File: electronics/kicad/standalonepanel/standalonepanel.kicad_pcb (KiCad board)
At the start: 2 copper layers, 135 x 54 mm, 81 parts, among them J1 Speaker, J2 POWER, P1 USB-C, P2 USB-A, SW1 TST-ESP32, SW2 BOOT, SW3 TST-ICE40, SW4 RESET, U1 SC189ZSKTRT, U10 MPU-6050, U2 SC189ZSKTRT, U3 ESP32-WROVER-E, U4 CH340C, U5 MAX3421E, U6 IS64WV25616EFBLL-10TLI, U7 ICE40-HX4K, U9 MAX98357A, X2 12MHz

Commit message: electronics & PCB v1
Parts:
- added BT1: CR2032, 0_project:cr2032_smd_clip, F.Cu at (120.7, 99.3)
- added C14: 100nF, Capacitor_SMD:C_0805_2012Metric_Pad1.18x1.45mm_HandSolder, B.Cu at (151.5, 117.5)
- added R9: 10K, Resistor_SMD:R_1206_3216Metric_Pad1.30x1.75mm_HandSolder, B.Cu at (116.7, 128.1)
- added U8: DS3231M, Package_SO:SO-16_3.9x9.9mm_P1.27mm, F.Cu at (151.0, 117.5)
- moved G*** 33.0 mm to (100.6, 106.0)
- moved C27 25.7 mm to (141.8, 114.8), turned to 90 degrees
- moved R15 22.5 mm to (137.8, 114.0)
- moved SW4 12.6 mm to (137.7, 110.4), turned to 180 degrees
- moved LED3 2.83 mm to (137.6, 117.5)
- moved LED1 2.77 mm to (137.7, 123.4)
- moved R5 2.62 mm to (137.8, 126.0)
- moved R8 2.46 mm to (137.7, 120.0)
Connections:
- net /DSP1_B1 renamed DSP1-B1
- net /DSP1_B2 renamed DSP1-B2
- net /DSP1_G1 renamed DSP1-G1
- net /DSP1_G2 renamed DSP1-G2
- net /DSP1_R1 renamed DSP1-R1
- net /DSP1_R2 renamed DSP1-R2
- net /DSP2_B1 renamed DSP2-B1
- net /DSP2_B2 renamed DSP2-B2
- net /DSP2_G1 renamed DSP2-G1
- net /DSP2_G2 renamed DSP2-G2
- net /DSP2_R1 renamed DSP2-R1
- net /DSP2_R2 renamed DSP2-R2
- net /DSP_A renamed DSP-A
- net /DSP_B renamed DSP-B
- net /DSP_C renamed DSP-C
- net /DSP_CLK renamed DSP-CLK
- net /DSP_D renamed DSP-D
- net /DSP_E renamed DSP-E
- net /DSP_LAT renamed DSP-LAT
- net /DSP_OE renamed DSP-OE
- net /HSPI-CLK renamed HSPI-CLK
- net /HSPI-CS-USB renamed HSPI-CS-USB
- net /HSPI-SDI renamed HSPI-SDI
- net /HSPI-SDO renamed HSPI-SDO
- net /HSPI_INT renamed HSPI-INT
- net /I2C-CLK renamed I2C-CLK
- net /I2C-SDA renamed I2C-SDA
- net /ICE40-CDONE renamed Net-(LED4-A)
- net /RAM-A0 renamed RAM-A0
- net /RAM-A1 renamed RAM-A1
- net /RAM-A10 renamed RAM-A10
- net /RAM-A11 renamed RAM-A11
- net /RAM-A12 renamed RAM-A12
- net /RAM-A13 renamed RAM-A13
- net /RAM-A14 renamed RAM-A14
- net /RAM-A15 renamed RAM-A15
- net /RAM-A16 renamed RAM-A16
- net /RAM-A17 renamed RAM-A17
- net /RAM-A2 renamed RAM-A2
- net /RAM-A3 renamed RAM-A3
- net /RAM-A4 renamed RAM-A4
- net /RAM-A5 renamed RAM-A5
- net /RAM-A6 renamed RAM-A6
- net /RAM-A7 renamed RAM-A7
- net /RAM-A8 renamed RAM-A8
- net /RAM-A9 renamed RAM-A9
- net /RAM-CS renamed RAM-CS
- net /RAM-D0 renamed RAM-D0
- net /RAM-D1 renamed RAM-D1
- net /RAM-D10 renamed RAM-D10
- net /RAM-D11 renamed RAM-D11
- net /RAM-D12 renamed RAM-D12
- net /RAM-D13 renamed RAM-D13
- net /RAM-D14 renamed RAM-D14
- net /RAM-D15 renamed RAM-D15
- net /RAM-D2 renamed RAM-D2
- net /RAM-D3 renamed RAM-D3
- net /RAM-D4 renamed RAM-D4
- net /RAM-D5 renamed RAM-D5
- net /RAM-D6 renamed RAM-D6
- net /RAM-D7 renamed RAM-D7
- net /RAM-D8 renamed RAM-D8
- net /RAM-D9 renamed RAM-D9
- net /RAM-OE renamed RAM-OE
- net /RAM-WE renamed RAM-WE
- net /SYSCLK renamed SYSCLK
- net /VSPI-SDO renamed VSPI-SDO
- net /~{ICE40-RESET} renamed ~{ICE40-RESET}
- net /~{RESET} renamed ~{RESET}
- U3 pad 10: /VSPI-CS-FLSH -> VSPI-SDI
- U3 pad 11: /VSPI-SDI -> unconnected-(U3-DAC_2/ADC2_CH9/GPIO26-Pad11)
- U3 pad 33: /VSPI-CLK -> VSPI-CLK
- U3 pad 37: /VSPI-CS-ICE -> unconnected-(U3-GPIO23-Pad37)
- U7 pad 62: /VSPI-CS-ICE -> unconnected-(U7-IOB_102-Pad62)
- U7 pad 68: /VSPI-CLK -> VSPI-SDI
- U7 pad 70: unconnected-(U7-IOB_107_SCK-Pad70) -> VSPI-CLK
- U7 pad 71: unconnected-(U7-IOB_108_SS-Pad71) -> Net-(U7-IOB_108_SS)
- U7 pad 78: /VSPI-SDI -> unconnected-(U7-IOR_114-Pad78)
- U7 pad 79: /VSPI-CS-FLSH -> unconnected-(U7-IOR_115-Pad79)
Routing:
- net /VSPI-CS-ICE: track 103.9 -> 0.00 mm
- net Net-(BT1-+): track 0.00 -> 58.9 mm, vias 0 -> 2
- net /VSPI-CLK: track 57.6 -> 0.00 mm, vias 2 -> 0
- net VSPI-CLK: track 0.00 -> 56.6 mm, vias 0 -> 2
- net VSPI-SDI: track 0.00 -> 51.8 mm, vias 0 -> 2
- net /VSPI-CS-FLSH: track 43.2 -> 0.00 mm, vias 2 -> 0
- net /VSPI-SDI: track 42.0 -> 0.00 mm, vias 2 -> 0
- net Net-(C27-Pad1): track 53.5 -> 32.0 mm
- net GND: track 809.2 -> 830.6 mm, vias 22 -> 23
- net I2C-CLK: track 46.0 -> 65.4 mm, vias 0 -> 2
- net I2C-SDA: track 43.2 -> 60.5 mm, vias 2 -> 3
- net +3V3: track 382.5 -> 398.9 mm, vias 15 -> 16
- net Net-(U7-IOB_108_SS): track 0.00 -> 8.56 mm, vias 0 -> 1
- net Net-(U7-IOR_110): track 7.58 -> 15.0 mm
- net Net-(U7-IOR_112): track 12.6 -> 7.96 mm
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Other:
- outline, holes or cut-outs redrawn
- board text added: "Standalonepanel v1 EvO Apr.2024"
- board text removed: "Standalonepanel v1.0 EvO Mar.2024"

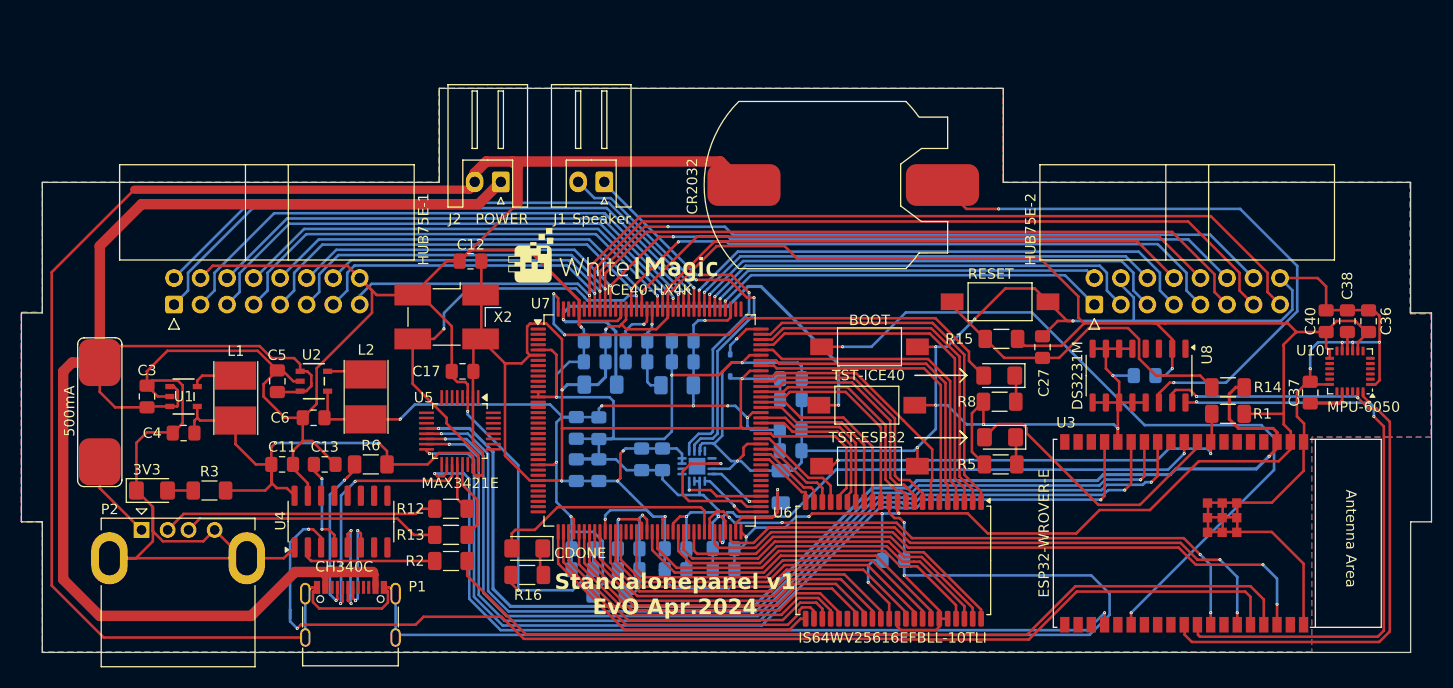
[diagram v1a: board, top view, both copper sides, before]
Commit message: fix schematic errors: - swapped TxD/RxD + resistor CH340 - corrected footprint of DS3231 (was too big) textual errors of U2 (C-variant 1.2V)
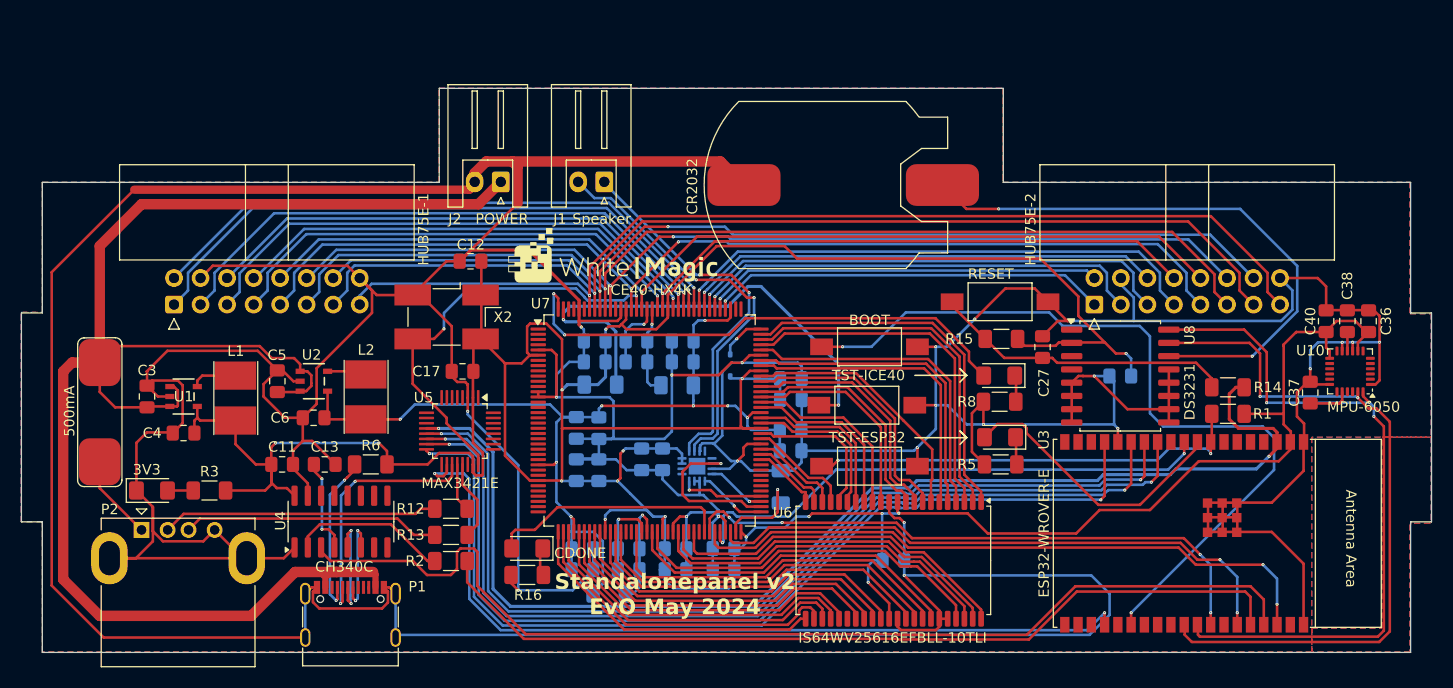
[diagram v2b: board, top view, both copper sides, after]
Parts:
- D2: value 1N5819WS -> BAT760
- R2: value 33R -> 47R
- U2: value SC189ZSKTRT -> SC189CSKTRT
- U8: value DS3231M -> DS3231; footprint Package_SO:SO-16_3.9x9.9mm_P1.27mm -> Package_SO:SOIC-16W_7.5x10.3mm_P1.27mm
- moved C14 2.34 mm to (149.2, 117.5)
- moved U8 1.80 mm to (149.2, 117.5), turned to 0 degrees
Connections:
- R2 pad 1: Net-(U3-U0TXD/GPIO1) -> Net-(U3-U0RXD/GPIO3)
- U4 pad 3: Net-(U3-U0RXD/GPIO3) -> Net-(U3-U0TXD/GPIO1)
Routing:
- net Net-(U3-U0RXD/GPIO3): track 111.6 -> 84.1 mm, vias 2 -> 0
- net +3V3: track 398.9 -> 379.5 mm
- net Net-(U3-U0TXD/GPIO1): track 84.9 -> 103.8 mm
- net I2C-SDA: track 60.5 -> 67.8 mm
- net GND: track 830.6 -> 836.3 mm
- net Net-(U3-GPIO0/BOOT/ADC2_CH1): track 73.2 -> 77.5 mm
- net I2C-CLK: track 65.4 -> 68.7 mm
- net Net-(BT1-+): track 58.9 -> 55.6 mm
- net Net-(C27-Pad1): track 32.0 -> 29.0 mm
- net Net-(U4-TXD): track 13.3 -> 15.2 mm
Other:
- board text added: "Standalonepanel v2 EvO May 2024"
- board text removed: "Standalonepanel v1 EvO Apr.2024"

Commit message: changed I2C address of MPU6050 from 0x68 to 0x69 to remove conflict with DS3231
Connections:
- U10 pad 9: GND -> +3V3
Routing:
- net GND: track 836.3 -> 835.5 mm, vias 23 -> 22
- net +3V3: track 379.5 -> 380.0 mm
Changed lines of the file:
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@@
 			(layers "F.Cu" "F.Paste" "F.Mask")
 			(roundrect_rratio 0.25)
-			(net 2 "GND")
+			(net 36 "+3V3")
 			(pinfunction "AD0")
 			(pintype "input")
@@
 	)
 	(segment
-		(start 171.446 115.144)
-		(end 171.446 114.304)
-		(width 0.25)
-		(layer "F.Cu")
-		(net 2)
-	)
-	(segment
 		(start 160.404 132.464)
 		(end 157.604 132.464)
@@
 	)
 	(segment
-		(start 171.446 114.304)
-		(end 171.45 114.3)
-		(width 0.25)
-		(layer "F.Cu")
-		(net 2)
-	)
-	(segment
 		(start 159.004 132.464)
 		(end 159.004 129.664)
@@
 	)
 	(via micro
-		(at 171.446 114.304)
-		(size 0.3)
-		(drill 0.1)
-		(layers "F.Cu" "B.Cu")
-		(net 2)
-	)
-	(via micro
 		(at 170.446 114.312)
 		(size 0.3)
@@
 		(width 0.25)
 		(layer "F.Cu")
+		(net 36)
+	)
+	(segment
+		(start 171.946 115.144)
+		(end 171.446 115.144)
+		(width 0.25)
+		(layer "F.Cu")

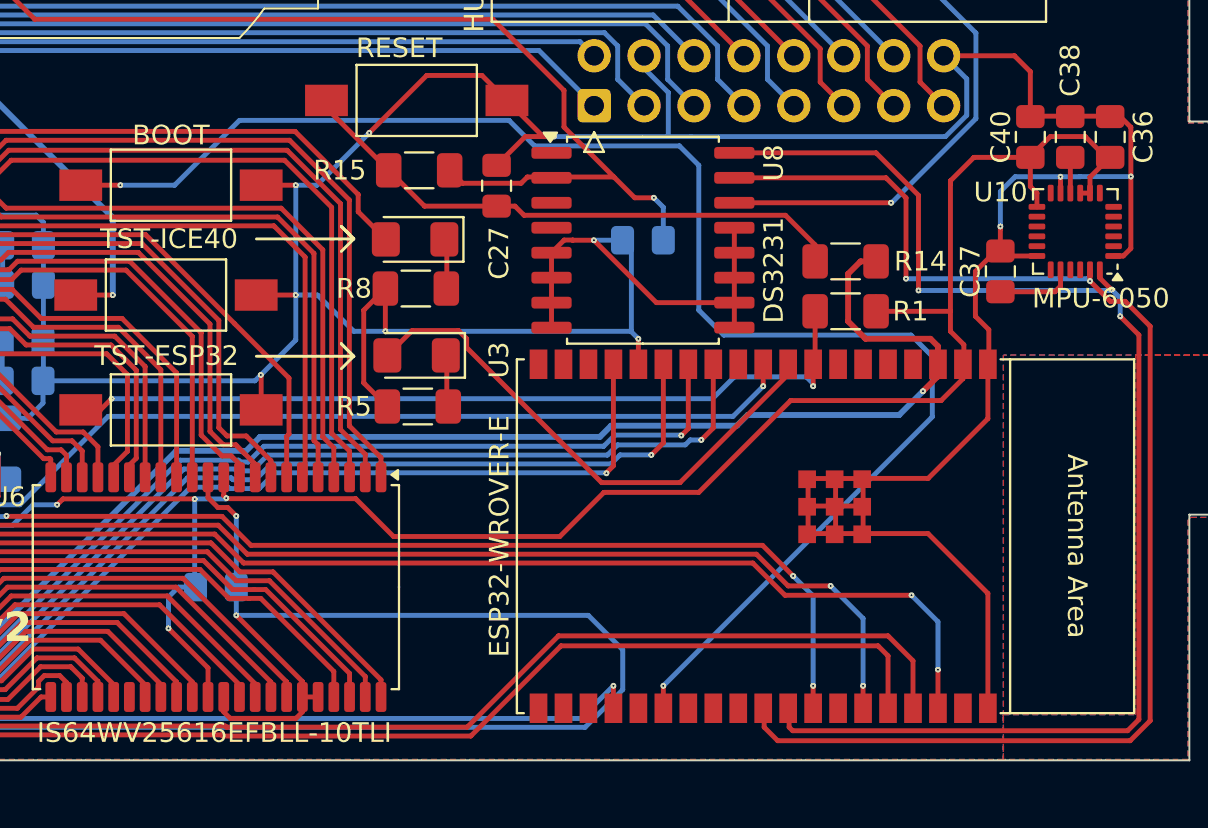
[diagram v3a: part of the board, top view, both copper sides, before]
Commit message: added SDA and SCL pullup resistors swapped teh SDA and SCL lines for DS3231
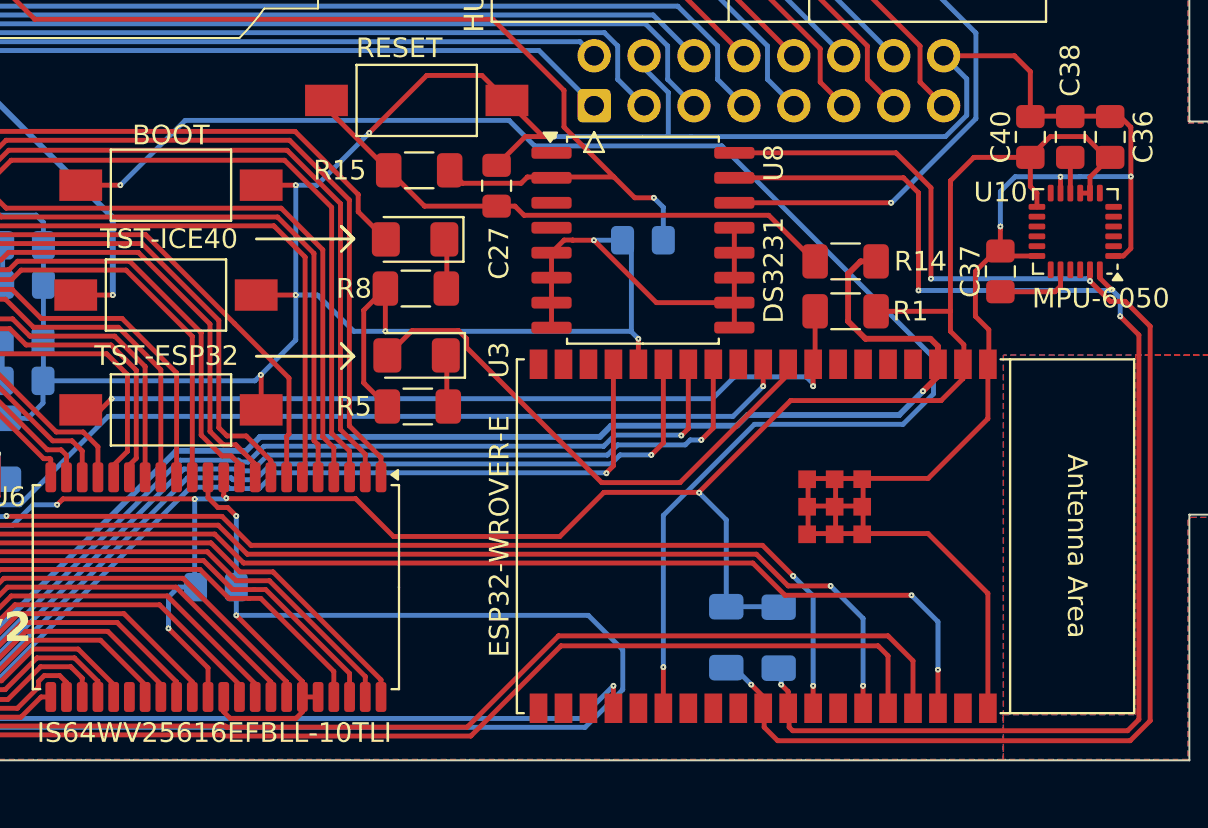
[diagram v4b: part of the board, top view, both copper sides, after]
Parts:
- added R10: 2K7, Resistor_SMD:R_1206_3216Metric_Pad1.30x1.75mm_HandSolder, B.Cu at (153.4, 137.7)
- added R11: 2K7, Resistor_SMD:R_1206_3216Metric_Pad1.30x1.75mm_HandSolder, B.Cu at (156.1, 137.8)
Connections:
- U8 pad 15: I2C-CLK -> I2C-SDA
- U8 pad 16: I2C-SDA -> I2C-CLK
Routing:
- net +3V3: track 380.0 -> 389.1 mm, vias 16 -> 17
- net I2C-CLK: track 68.7 -> 72.6 mm, vias 2 -> 3
- net I2C-SDA: track 67.8 -> 69.6 mm, vias 3 -> 4

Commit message: Schematic v2 PCB version v2 send for production
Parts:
- removed F1: 500mA, 0_project:FUSEHOLDER 1808
- removed P1: USB-C, 0_project:USB_C_Receptacle_G-Switch_GT-USB-7010ASV
- removed P2: USB-A, 0_project:USB-A TH Female
- removed X2: 12MHz, 0_project:Oscillator_SMD_EuroQuartz_XO91-4Pin_7.0x5.0mm_HandSoldering
- added C39: 100nF, Capacitor_SMD:C_0805_2012Metric_Pad1.18x1.45mm_HandSolder, B.Cu at (101.2, 128.2)
- added C41: 4.7uF, Capacitor_SMD:C_0805_2012Metric_Pad1.18x1.45mm_HandSolder, B.Cu at (105.2, 128.2)
- added C42: 100nF, Capacitor_SMD:C_0805_2012Metric_Pad1.18x1.45mm_HandSolder, F.Cu at (171.0, 110.8)
- added C43: 2.2nF/50V, Capacitor_SMD:C_0805_2012Metric_Pad1.18x1.45mm_HandSolder, F.Cu at (167.5, 116.2)
- added C44: 100nF, Capacitor_SMD:C_0805_2012Metric_Pad1.18x1.45mm_HandSolder, F.Cu at (139.8, 120.0)
- added C45: 100nF, Capacitor_SMD:C_0805_2012Metric_Pad1.18x1.45mm_HandSolder, F.Cu at (158.2, 115.8)
- added D1: P4SMA27A, Diode_SMD:D_SMA_Handsoldering, F.Cu at (53.2, 115.2)
- added D3: BAT760, Diode_SMD:D_SOD-323, F.Cu at (68.8, 121.8)
- added D4: P4SMA27A, Diode_SMD:D_SMA_Handsoldering, F.Cu at (52.0, 129.5)
- added D5: P4SMA27A, Diode_SMD:D_SMA_Handsoldering, F.Cu at (64.5, 140.5)
- added D6: P4SMA27A, Diode_SMD:D_SMA_Handsoldering, F.Cu at (64.5, 136.8)
- added J3: Speaker, Connector_JST:JST_XH_S2B-XH-A_1x02_P2.50mm_Horizontal, F.Cu at (89.2, 99.5)
- added LED5: CDONE, LED_SMD:LED_1206_3216Metric_Pad1.42x1.75mm_HandSolder, F.Cu at (94.0, 134.5)
- added Q1: AO4435, Package_SO:SOIC-8_3.9x4.9mm_P1.27mm, F.Cu at (52.0, 124.2)
- added R18: 10K, Resistor_SMD:R_1206_3216Metric_Pad1.30x1.75mm_HandSolder, B.Cu at (108.5, 124.8)
- added R19: 22R, Resistor_SMD:R_1206_3216Metric_Pad1.30x1.75mm_HandSolder, F.Cu at (94.0, 132.2)
- added R20: 100R, Resistor_SMD:R_1206_3216Metric_Pad1.30x1.75mm_HandSolder, B.Cu at (103.5, 124.8)
- added R21: 10K, Resistor_SMD:R_1206_3216Metric_Pad1.30x1.75mm_HandSolder, F.Cu at (163.8, 113.5)
- added R22: 100R, Resistor_SMD:R_1206_3216Metric_Pad1.30x1.75mm_HandSolder, F.Cu at (158.8, 113.5)
- added R23: 2K7, Resistor_SMD:R_1206_3216Metric_Pad1.30x1.75mm_HandSolder, F.Cu at (139.6, 125.5)
- added R24: 2K7, Resistor_SMD:R_1206_3216Metric_Pad1.30x1.75mm_HandSolder, F.Cu at (142.0, 125.5)
- added SW5: TST-ICE40, Button_Switch_SMD:SW_SPST_FSMSM, F.Cu at (124.8, 114.2)
- added SW6: RESET, Button_Switch_SMD:SW_SPST_FSMSM, F.Cu at (150.2, 115.2)
- added X1: 12MHz, 0_project:Oscillator_SMD_EuroQuartz_XO91-4Pin_7.0x5.0mm_HandSoldering, F.Cu at (82.5, 121.5)
- C14, C25, C29, C33, R7: moved to F.Cu
- C15, C20: value 100nF -> 1uF; moved to F.Cu
- C16, C19, C21: value 4.7uF -> 1uF; moved to F.Cu
- C17: value 1uF -> 100nF; moved to B.Cu
- C18, C31, C34: value 100nF -> 4.7uF
- C23: value 10uF -> 4.7uF
- C27, C40: moved to B.Cu
- C28: value 4.7uF -> 10uF; moved to F.Cu
- C30, C35: value 4.7uF -> 100nF
- C32: value 4.7uF -> 10nF; moved to F.Cu
- C36: value 10nF -> 4.7uF; moved to B.Cu
- C37: value 2.2nF/50V -> 100nF; moved to B.Cu
- C38: value 100nF -> 4.7uF; moved to B.Cu
- J1: value Speaker -> LEDPWR; footprint Connector_JST:JST_XH_S2B-XH-A_1x02_P2.50mm_Horizontal -> 0_project:JST_VH_1x04_P3.96mm_Horizontal
- J2: value POWER -> USB_C-PD; footprint Connector_JST:JST_XH_S2B-XH-A_1x02_P2.50mm_Horizontal -> 0_project:USB_C_Receptacle_G-Switch_GT-USB-7010ASV
- LED1: value ESP32 -> 3V3
- LED2: value 3V3 -> ESP32
- LED4: value CDONE -> PD
- R1: value 10K -> 1K5
- R10: value 2K7 -> 100K; moved to F.Cu
- R11: value 2K7 -> 1K; moved to F.Cu
- R12: value 33R -> 100R
- R13: value 33R -> 470R
- R14: value 100R -> 22K
- R15: value 10K -> 1K
- R16: value 22R -> 1K5
- R17: value 100R -> 10K; moved to F.Cu
- R2: value 47R -> 10K
- R3: value 1K5 -> 47R
- R6: value 5K1 -> 10K
- R8: value 2K2 -> 10K
- R9: value 10K -> 2K2; moved to F.Cu
- SW1: value TST-ESP32 -> SET; footprint Button_Switch_SMD:SW_SPST_FSMSM -> 0_project:SW_Tactile_SKHH_Angled
- SW3: value TST-ICE40 -> UP; footprint Button_Switch_SMD:SW_SPST_FSMSM -> 0_project:SW_Tactile_SKHH_Angled
- SW4: value RESET -> DOWN; footprint Button_Switch_SMD:SW_SPST_FSMSM -> 0_project:SW_Tactile_SKHH_Angled
- U10: value MPU-6050 -> DS3231; footprint 0_project:InvenSense_QFN-24_4x4mm_P0.5mm -> Package_SO:SOIC-16W_7.5x10.3mm_P1.27mm
- U3: value ESP32-WROVER-E -> CH340C; footprint 0_project:ESP32-WROVER-E -> Package_SO:SOIC-16_3.9x9.9mm_P1.27mm
- U4: value CH340C -> ESP32-WROVER-E; footprint Package_SO:SOIC-16_3.9x9.9mm_P1.27mm -> 0_project:ESP32-WROVER-E
- U5: value MAX3421E -> IS64WV25616EFBLL-10TLI; footprint 0_project:PQFP-32_5x5mm_P0.5mm -> Package_SO:TSOP-II-44_10.16x18.41mm_P0.8mm
- U6: value IS64WV25616EFBLL-10TLI -> STUSB4500QTR; footprint Package_SO:TSOP-II-44_10.16x18.41mm_P0.8mm -> 0_project:QFN-24-1EP_4x4mm_P0.5mm_EP2.7x2.7mm
- U8: value DS3231 -> MAX98357A; footprint Package_SO:SOIC-16W_7.5x10.3mm_P1.27mm -> Package_DFN_QFN:TQFN-16-1EP_3x3mm_P0.5mm_EP1.6x1.6mm
- U9: value MAX98357A -> MPU-6050; footprint Package_DFN_QFN:TQFN-16-1EP_3x3mm_P0.5mm_EP1.6x1.6mm -> 0_project:InvenSense_QFN-24_4x4mm_P0.5mm; moved to F.Cu
- moved LED2 102.6 mm to (158.8, 121.2)
- moved R14 98.5 mm to (61.8, 131.0), turned to 0 degrees
- moved R10 95.9 mm to (58.0, 128.8)
- moved R11 94.9 mm to (61.7, 128.5), turned to 0 degrees
- moved U4 86.1 mm to (160.7, 132.6), turned to -90 degrees
- moved C14 84.8 mm to (65.8, 132.8), turned to -90 degrees
- moved R1 83.8 mm to (75.8, 119.2), turned to 90 degrees
- moved U3 76.3 mm to (85.1, 111.8), turned to 90 degrees
- moved C38 73.4 mm to (99.2, 128.2)
- moved C32 70.4 mm to (173.0, 110.8), turned to -90 degrees
- moved R15 69.4 mm to (68.5, 117.9), turned to -90 degrees
- moved C40 67.6 mm to (103.2, 128.2)
- moved C33 67.3 mm to (169.0, 110.8), turned to -90 degrees
- moved C15 67.2 mm to (51.8, 132.8), turned to 180 degrees
- moved U6 66.4 mm to (62.0, 124.2), turned to 0 degrees
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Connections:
- C12 pad 1: +3V3 -> Net-(U3-V3)
- C13 pad 1: Net-(U4-V3) -> +3V3
- C14 pad 1: GND -> VPANEL
- C14 pad 2: +3V3 -> Net-(C14-Pad2)
- C15 pad 1: +3V3 -> VBUS
- C16 pad 1: +3V3 -> Net-(D3-K)
- C17 pad 1: GND -> +3V3
- C17 pad 2: +3V3 -> GND
- C18 pad 1: +1V2 -> +3V3
- C19 pad 1: +1V2 -> Net-(U6-VREG_2V7)
- C20 pad 1: +3V3 -> Net-(U6-VREG_1V2)
- C21 pad 1: GND -> VBUS
- C21 pad 2: +1V2 -> GND
- C22 pad 1: GND -> +1V2
- C22 pad 2: +1V2 -> GND
- C23 pad 1: +3V3 -> +1V2
- C25 pad 2: GND -> Net-(U6-RESET)
- C26 pad 1: +3V3 -> GND
- C26 pad 2: GND -> +1V2
- C27 pad 1: Net-(C27-Pad1) -> GND
- C27 pad 2: GND -> +1V2
- C28 pad 1: GND -> +3V3
- C28 pad 2: +1V2 -> GND
- C29 pad 1: GND -> +3V3
- C29 pad 2: +1V2 -> GND
- C3 pad 1: +5V -> VBUS
- C30 pad 1: GND -> +3V3
- C30 pad 2: +3V3 -> GND
- C31 pad 1: GND -> +3V3
- C31 pad 2: +3V3 -> GND
- C34 pad 1: Net-(U7-VCCPLL0) -> GND
- C34 pad 2: Net-(U7-GNDPLL0) -> +3V3
- C35 pad 1: Net-(U7-VCCPLL0) -> GND
- C35 pad 2: Net-(U7-GNDPLL0) -> +3V3
- C37 pad 2: Net-(U10-CPOUT) -> +3V3
- C38 pad 2: Net-(U10-REGOUT) -> +1V2
- C40 pad 1: GND -> Net-(U7-VCCPLL0)
- C40 pad 2: +3V3 -> Net-(U7-GNDPLL0)
- C5 pad 1: +5V -> VBUS
- J1 pad 1: Net-(J1-Pin_1) -> VPANEL
- J1 pad 2: Net-(J1-Pin_2) -> VPANEL
- LED1 pad 1: Net-(LED1-K) -> GND
- R1 pad 1: +3V3 -> Net-(LED1-A)
- R1 pad 2: Net-(U3-32K_XP/GPIO32/ADC1_CH4) -> +3V3
- R10 pad 1: +3V3 -> VBUS
- R10 pad 2: I2C-CLK -> Net-(Q1-G1)
- R11 pad 1: +3V3 -> VPANEL
- R11 pad 2: I2C-SDA -> Net-(U6-DISCH)
- R12 pad 1: Net-(P2-D-) -> Net-(C14-Pad2)
- R12 pad 2: Net-(U5-D-) -> Net-(Q1-G1)
- R13 pad 1: Net-(P2-D+) -> VBUS
- R13 pad 2: Net-(U5-D+) -> Net-(D3-K)
- R14 pad 1: ~{RESET} -> Net-(Q1-G1)
- R14 pad 2: Net-(C27-Pad1) -> Net-(U6-VBUS_EN_SNK)
- R15 pad 1: +3V3 -> Net-(D3-K)
- R15 pad 2: Net-(C27-Pad1) -> Net-(U6-VBUS_VS_DISCH)
- R16 pad 1: Net-(LED4-K) -> Net-(LED4-A)
- R16 pad 2: GND -> +3V3
- R17 pad 1: Net-(U7-VCCPLL0) -> Net-(U6-RESET)
- R17 pad 2: +1V2 -> GND
- R2 pad 1: Net-(U3-U0RXD/GPIO3) -> +3V3
- R2 pad 2: Net-(U4-TXD) -> Net-(U4-32K_XP/GPIO32/ADC1_CH4)
- R3 pad 1: Net-(LED2-A) -> Net-(U4-U0RXD/GPIO3)
- R3 pad 2: +3V3 -> Net-(U3-TXD)
- R5 pad 1: Net-(LED1-K) -> Net-(U4-32K_XN/GPIO33/ADC1_CH5)
- R5 pad 2: GND -> Net-(LED2-A)
- R6 pad 1: Net-(P1-CC) -> +3V3
- R6 pad 2: +3V3 -> Net-(U4-GPIO35/ADC1_CH7)
- R7 pad 2: Net-(U7-IOT_221) -> Net-(U4-GPIO34/ADC1_CH6)
- R8 pad 1: Net-(LED3-K) -> +3V3
- R8 pad 2: GND -> Net-(U7-IOT_221)
- R9 pad 1: Net-(U7-IOB_108_SS) -> Net-(LED3-K)
- SW1 pad 2: Net-(U3-32K_XP/GPIO32/ADC1_CH4) -> Net-(U4-32K_XP/GPIO32/ADC1_CH4)
- SW2 pad 1: Net-(U3-GPIO0/BOOT/ADC2_CH1) -> Net-(U4-GPIO0/BOOT/ADC2_CH1)
- SW3 pad 2: Net-(U7-IOT_221) -> Net-(U4-GPIO35/ADC1_CH7)
- SW4 pad 2: Net-(C27-Pad1) -> Net-(U4-GPIO34/ADC1_CH6)
- U1 pad 1: +5V -> VBUS
- U1 pad 3: +5V -> VBUS
- U10 pad 1: GND -> unconnected-(U10-32KHZ-Pad1)
- U10 pad 10: Net-(U10-REGOUT) -> GND
- U10 pad 12: unconnected-(U10-INT-Pad12) -> GND
- U10 pad 13: +3V3 -> GND
- U10 pad 14: unconnected-(U10-NC-Pad14) -> Net-(BT1-+)
- U10 pad 15: unconnected-(U10-NC-Pad15) -> I2C-SDA
- U10 pad 16: unconnected-(U10-NC-Pad16) -> I2C-CLK
- U10 pad 2: unconnected-(U10-NC-Pad2) -> +3V3
- U10 pad 5: unconnected-(U10-NC-Pad5) -> GND
- U10 pad 6: unconnected-(U10-AUX_DA-Pad6) -> GND
- U10 pad 7: unconnected-(U10-AUX_CL-Pad7) -> GND
- U10 pad 8: +3V3 -> GND
- U10 pad 9: +3V3 -> GND
- U2 pad 1: +5V -> VBUS
- U2 pad 3: +5V -> VBUS
- U3 pad 10: VSPI-SDI -> unconnected-(U3-~{DSR}-Pad10)
- U3 pad 12: HSPI-CS-USB -> unconnected-(U3-~{DCD}-Pad12)
- U3 pad 13: HSPI-CLK -> unconnected-(U3-~{DTR}-Pad13)
- U3 pad 14: HSPI-SDO -> unconnected-(U3-~{RTS}-Pad14)
- U3 pad 16: HSPI-SDI -> +3V3
- U3 pad 2: +3V3 -> Net-(U3-TXD)
- U3 pad 3: ~{RESET} -> Net-(U3-RXD)
- U3 pad 4: unconnected-(U3-SENSOR_VP/GPIO36/ADC1_CH0-Pad4) -> Net-(U3-V3)
- U3 pad 5: unconnected-(U3-SENSOR_VN/GPIO39/ADC1_CH3-Pad5) -> Net-(U3-UD+)
- U3 pad 6: unconnected-(U3-GPIO34/ADC1_CH6-Pad6) -> Net-(U3-UD-)
- U3 pad 8: Net-(U3-32K_XP/GPIO32/ADC1_CH4) -> unconnected-(U3-NC-Pad8)
- U3 pad 9: Net-(LED1-A) -> unconnected-(U3-~{CTS}-Pad9)
- U4 pad 10: unconnected-(U4-~{DSR}-Pad10) -> VSPI-SDI
- U4 pad 16: +3V3 -> unconnected-(U4-MTCK/GPIO13/ADC2_CH4-Pad16)
- U4 pad 2: Net-(U4-TXD) -> +3V3
- U4 pad 3: Net-(U3-U0TXD/GPIO1) -> ~{RESET}
- U4 pad 4: Net-(U4-V3) -> unconnected-(U4-SENSOR_VP/GPIO36/ADC1_CH0-Pad4)
- U4 pad 5: Net-(P1-D+) -> unconnected-(U4-SENSOR_VN/GPIO39/ADC1_CH3-Pad5)
- U4 pad 6: Net-(P1-D-) -> Net-(U4-GPIO34/ADC1_CH6)
- U4 pad 7: unconnected-(U4-NC-Pad7) -> Net-(U4-GPIO35/ADC1_CH7)
- U4 pad 8: unconnected-(U4-NC-Pad8) -> Net-(U4-32K_XP/GPIO32/ADC1_CH4)
- U4 pad 9: unconnected-(U4-~{CTS}-Pad9) -> Net-(U4-32K_XN/GPIO33/ADC1_CH5)
- U5 pad 1: unconnected-(U5-GPIN7-Pad1) -> RAM-A0
- U5 pad 10: unconnected-(U5-GPOUT6-Pad10) -> RAM-D3
- U5 pad 11: unconnected-(U5-GPOUT7-Pad11) -> +3V3
- U5 pad 12: ~{RESET} -> GND
- U5 pad 13: HSPI-CLK -> RAM-D4
- U5 pad 14: HSPI-CS-USB -> RAM-D5
- U5 pad 15: HSPI-SDO -> RAM-D6
- U5 pad 16: HSPI-SDI -> RAM-D7
- U5 pad 17: unconnected-(U5-GPX-Pad17) -> RAM-WE
- U5 pad 18: HSPI-INT -> RAM-A5
- U5 pad 19: (no net) -> RAM-A6
- U5 pad 2: +3V3 -> RAM-A1
- U5 pad 20: Net-(U5-D-) -> RAM-A7
- U5 pad 21: Net-(U5-D+) -> RAM-A8
- U5 pad 22: unconnected-(U5-VBCOMP-Pad22) -> RAM-A9
- U5 pad 23: +3V3 -> RAM-A10
- U5 pad 24: SYSCLK -> RAM-A11
- U5 pad 25: unconnected-(U5-XO-Pad25) -> RAM-A12
- U5 pad 26: unconnected-(U5-GPIN0-Pad26) -> RAM-A13
- U5 pad 27: unconnected-(U5-GPIN1-Pad27) -> RAM-A14
- U5 pad 29: unconnected-(U5-GPIN3-Pad29) -> RAM-D8
- U5 pad 3: GND -> RAM-A2
- U5 pad 30: unconnected-(U5-GPIN4-Pad30) -> RAM-D9
- U5 pad 31: unconnected-(U5-GPIN5-Pad31) -> RAM-D10
- U5 pad 32: unconnected-(U5-GPIN6-Pad32) -> RAM-D11
- U5 pad 4: unconnected-(U5-GPOUT0-Pad4) -> RAM-A3
- U5 pad 5: unconnected-(U5-GPOUT1-Pad5) -> RAM-A4
- U5 pad 6: unconnected-(U5-GPOUT2-Pad6) -> RAM-CS
- U5 pad 7: unconnected-(U5-GPOUT3-Pad7) -> RAM-D0
- U5 pad 8: unconnected-(U5-GPOUT4-Pad8) -> RAM-D1
- U5 pad 9: unconnected-(U5-GPOUT5-Pad9) -> RAM-D2
- U6 pad 1: RAM-A0 -> Net-(D5-K)
- U6 pad 10: RAM-D3 -> GND
- U6 pad 11: +3V3 -> unconnected-(U6-ATTACH-Pad11)
- U6 pad 13: RAM-D4 -> GND
- U6 pad 14: RAM-D5 -> unconnected-(U6-POWER_OK3-Pad14)
- U6 pad 15: RAM-D6 -> unconnected-(U6-GPIO-Pad15)
- U6 pad 16: RAM-D7 -> Net-(U6-VBUS_EN_SNK)
- U6 pad 17: RAM-WE -> unconnected-(U6-A_B_SIDE-Pad17)
- U6 pad 18: RAM-A5 -> Net-(U6-VBUS_VS_DISCH)
- U6 pad 19: RAM-A6 -> Net-(LED4-K)
- U6 pad 2: RAM-A1 -> Net-(D5-K)
- U6 pad 20: RAM-A7 -> unconnected-(U6-POWER_OK2-Pad20)
- U6 pad 21: RAM-A8 -> Net-(U6-VREG_1V2)
- U6 pad 22: RAM-A9 -> GND
- U6 pad 23: RAM-A10 -> Net-(U6-VREG_2V7)
- U6 pad 24: RAM-A11 -> VBUS
- U6 pad 25: RAM-A12 -> GND
- U6 pad 3: RAM-A2 -> unconnected-(U6-NC-Pad3)
- U6 pad 4: RAM-A3 -> Net-(D6-K)
- U6 pad 5: RAM-A4 -> Net-(D6-K)
- U6 pad 6: RAM-CS -> Net-(U6-RESET)
- U6 pad 7: RAM-D0 -> I2C-CLK
- U6 pad 8: RAM-D1 -> I2C-SDA
- U6 pad 9: RAM-D2 -> Net-(U6-DISCH)
- U7 pad 15: unconnected-(U7-IOL_10A-Pad15) -> Net-(U7-IOL_10A)
- U7 pad 16: unconnected-(U7-IOL_10B-Pad16) -> Net-(U7-IOL_10B)
- U7 pad 17: unconnected-(U7-IOL_12A-Pad17) -> Net-(U7-IOL_12A)
- U7 pad 18: unconnected-(U7-IOL_12B-Pad18) -> Net-(U7-IOL_12B)
- U7 pad 65: Net-(LED4-A) -> Net-(LED5-A)
- U7 pad 73: Net-(U7-IOR_109) -> unconnected-(U7-IOR_109-Pad73)
- U7 pad 74: Net-(U7-IOR_110) -> unconnected-(U7-IOR_110-Pad74)
- U7 pad 75: Net-(U7-IOR_111) -> unconnected-(U7-IOR_111-Pad75)
- U7 pad 76: Net-(U7-IOR_112) -> unconnected-(U7-IOR_112-Pad76)
- U8 pad 1: unconnected-(U8-32KHZ-Pad1) -> Net-(U7-IOL_10B)
- U8 pad 10: GND -> Net-(J3-Pin_2)
- U8 pad 12: GND -> unconnected-(U8-NC-Pad12)
- U8 pad 13: GND -> unconnected-(U8-NC-Pad13)
- U8 pad 14: Net-(BT1-+) -> Net-(U7-IOL_12B)
- U8 pad 15: I2C-SDA -> GND
- U8 pad 16: I2C-CLK -> Net-(U7-IOL_12A)
- U8 pad 2: +3V3 -> GND
- U8 pad 3: unconnected-(U8-~{INT}/SQW-Pad3) -> GND
- U8 pad 4: unconnected-(U8-~{RST}-Pad4) -> Net-(U7-IOL_10A)
- U8 pad 5: GND -> unconnected-(U8-NC-Pad5)
- U8 pad 6: GND -> unconnected-(U8-NC-Pad6)
- U8 pad 7: GND -> +3V3
- U8 pad 8: GND -> +3V3
- U8 pad 9: GND -> Net-(J3-Pin_1)
- U9 pad 1: Net-(U7-IOR_109) -> GND
- U9 pad 10: Net-(J1-Pin_2) -> Net-(U9-REGOUT)
- U9 pad 13: unconnected-(U9-NC-Pad13) -> +3V3
- U9 pad 14: Net-(U7-IOR_110) -> unconnected-(U9-NC-Pad14)
- U9 pad 15: GND -> unconnected-(U9-NC-Pad15)
- U9 pad 16: Net-(U7-IOR_111) -> unconnected-(U9-NC-Pad16)
- U9 pad 17: (no net) -> unconnected-(U9-NC-Pad17)
- U9 pad 2: GND -> unconnected-(U9-NC-Pad2)
- U9 pad 3: GND -> unconnected-(U9-NC-Pad3)
- U9 pad 4: Net-(U7-IOR_112) -> unconnected-(U9-NC-Pad4)
- U9 pad 7: +3V3 -> unconnected-(U9-AUX_CL-Pad7)
- U9 pad 9: Net-(J1-Pin_1) -> +3V3
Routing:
- net GND: track 835.5 -> 664.8 mm, vias 22 -> 21
- net +5V: track 153.1 -> 0.00 mm
- net VBUS: track 0.00 -> 114.7 mm, vias 0 -> 3
- net I2C-SDA: track 69.6 -> 180.7 mm, vias 4 -> 6
- net Net-(U4-32K_XP/GPIO32/ADC1_CH4): track 0.00 -> 110.7 mm, vias 0 -> 2
- net I2C-CLK: track 72.6 -> 182.5 mm, vias 3 -> 6
- net Net-(U3-RXD): track 0.00 -> 107.9 mm, vias 0 -> 2
- net Net-(U3-U0TXD/GPIO1): track 103.8 -> 0.00 mm
- net Net-(U4-GPIO35/ADC1_CH7): track 0.00 -> 101.0 mm, vias 0 -> 2
- net ~{RESET}: track 113.4 -> 12.9 mm
- net VPANEL: track 0.00 -> 99.7 mm, vias 0 -> 2
- net HSPI-CS-USB: track 93.6 -> 0.00 mm, vias 2 -> 0
- net HSPI-CLK: track 92.2 -> 0.00 mm, vias 2 -> 0
- net HSPI-SDO: track 91.7 -> 0.00 mm, vias 2 -> 0
- net Net-(U4-GPIO34/ADC1_CH6): track 0.00 -> 91.3 mm, vias 0 -> 2
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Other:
- board text added: "+++"
- board text added: "GND"
- board text added: "Standalonepanel v2 EvO Sep 2024"
- board text removed: "Standalonepanel v2 EvO May 2024"

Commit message: added repeat of config selection
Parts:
- added U11: SN74LVC8T245, Package_SO:TSSOP-24_4.4x7.8mm_P0.65mm, F.Cu at (147.4, 89.4)
- added U12: SN74LVC8T245, Package_SO:TSSOP-24_4.4x7.8mm_P0.65mm, F.Cu at (156.5, 89.4)
- added U13: SN74LVC8T245, Package_SO:TSSOP-24_4.4x7.8mm_P0.65mm, F.Cu at (165.6, 89.4)
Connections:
- HUB75E-1 pad 1: DSP1-R1 -> DSP1-R1-5V
- HUB75E-1 pad 10: DSP-B -> DSP-B-5V
- HUB75E-1 pad 11: DSP-C -> DSP-C-5V
- HUB75E-1 pad 12: DSP-D -> DSP-D-5V
- HUB75E-1 pad 13: DSP-CLK -> DSP-CLK-5V
- HUB75E-1 pad 14: DSP-LAT -> DSP-LAT-5V
- HUB75E-1 pad 15: DSP-OE -> DSP-OE-5V
- HUB75E-1 pad 2: DSP1-G1 -> DSP1-G1-5V
- HUB75E-1 pad 3: DSP1-B1 -> DSP1-B1-5V
- HUB75E-1 pad 5: DSP1-R2 -> DSP1-R2-5V
- HUB75E-1 pad 6: DSP1-G2 -> DSP1-G2-5V
- HUB75E-1 pad 7: DSP1-B2 -> DSP1-B2-5V
- HUB75E-1 pad 8: DSP-E -> DSP-E-5V
- HUB75E-1 pad 9: DSP-A -> DSP-A-5V
- HUB75E-2 pad 1: DSP2-R1 -> DSP2-R1-5V
- HUB75E-2 pad 10: DSP-B -> DSP-B-5V
- HUB75E-2 pad 11: DSP-C -> DSP-C-5V
- HUB75E-2 pad 12: DSP-D -> DSP-D-5V
- HUB75E-2 pad 13: DSP-CLK -> DSP-CLK-5V
- HUB75E-2 pad 14: DSP-LAT -> DSP-LAT-5V
- HUB75E-2 pad 15: DSP-OE -> DSP-OE-5V
- HUB75E-2 pad 2: DSP2-G1 -> DSP2-G1-5V
- HUB75E-2 pad 3: DSP2-B1 -> DSP2-B1-5V
- HUB75E-2 pad 5: DSP2-R2 -> DSP2-R2-5V
- HUB75E-2 pad 6: DSP2-G2 -> DSP2-G2-5V
- HUB75E-2 pad 7: DSP2-B2 -> DSP2-B2-5V
- HUB75E-2 pad 8: DSP-E -> DSP-E-5V
- HUB75E-2 pad 9: DSP-A -> DSP-A-5V
